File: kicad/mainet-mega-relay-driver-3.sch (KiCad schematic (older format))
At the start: 10 parts, among them J36 Screw_Terminal_01x03, J86 Conn_01x01_Male, J87 Conn_01x01_Male, K3 SANYOU_SRD_Form_C, Q3 2N3904, U4 4N37

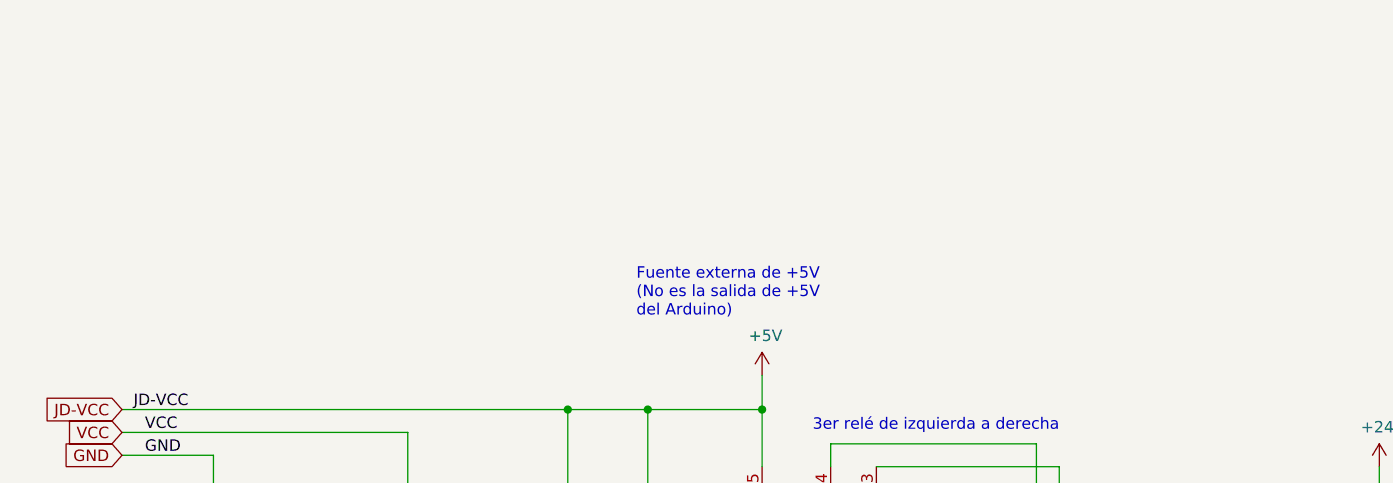
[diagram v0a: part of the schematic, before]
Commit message: KICAD: Actualizar .sch manejadores de relés Agrega alimentación de +5V de dispositivos del lado del Arduino diferente a la salida de +5V del Arduino
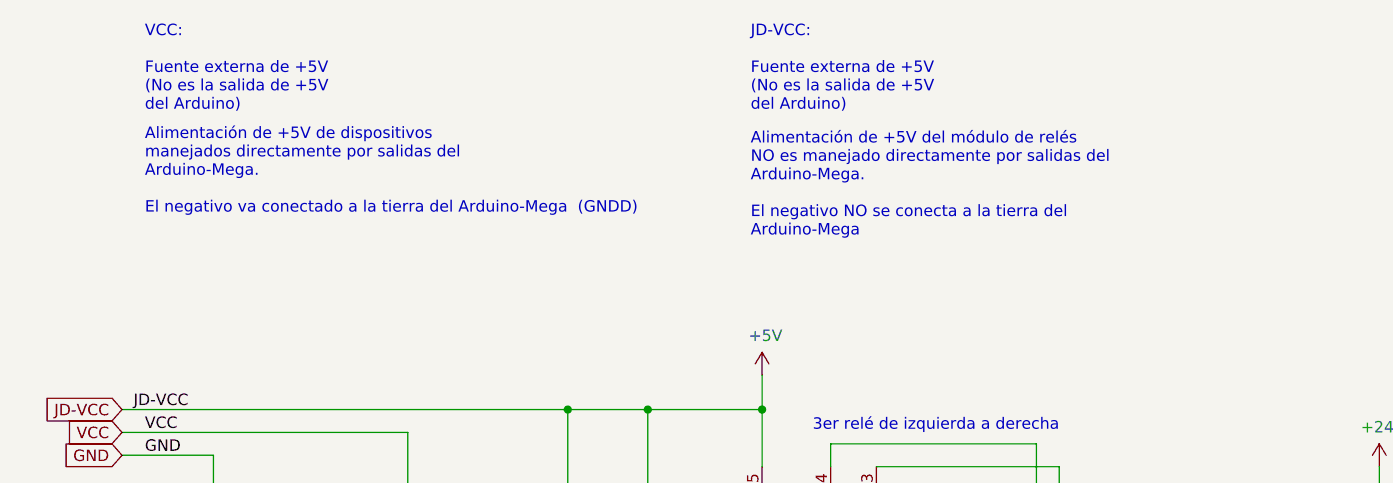
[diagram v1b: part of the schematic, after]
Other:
- note added: "Alimentación de +5V de dispositivos \nmanejados directamente por salidas del \nArduino-Mega.\n\nEl negativo va conectado a la tierra del Arduino-Mega (GNDD)"
- note added: "Alimentación de +5V del módulo de relés \nNO es manejado directamente por salidas del \nArduino-Mega.\n\nEl negativo NO se conecta a la tierra del \nArduino-Mega"
- note added: "JD-VCC:\n\nFuente externa de +5V\n(No es la salida de +5V \ndel Arduino)"
- note added: "VCC:\n\nFuente externa de +5V\n(No es la salida de +5V \ndel Arduino)"
- note removed: "Fuente externa de +5V\n(No es la salida de +5V \ndel Arduino)"
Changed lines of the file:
@@
 	1    0    0    -1
 $EndComp
-Text Notes 5900 2550 0    50   ~ 0
-Fuente externa de +5V\n(No es la salida de +5V \ndel Arduino)
 NoConn ~ 5500 4000
 Wire Wire Line
@@
 Wire Wire Line
 	9150 3300 9150 3700
+Text Notes 6400 1650 0    50   ~ 0
+JD-VCC:\n\nFuente externa de +5V\n(No es la salida de +5V \ndel Arduino)
+Text Notes 3750 1650 0    50   ~ 0
+VCC:\n\nFuente externa de +5V\n(No es la salida de +5V \ndel Arduino)
+Text Notes 3750 2100 0    50   ~ 0
+Alimentación de +5V de dispositivos \nmanejados directamente por salidas del \nArduino-Mega.\n\nEl negativo va conectado a la tierra del Arduino-Mega  (GNDD)
+Text Notes 6400 2200 0    50   ~ 0
+Alimentación de +5V del módulo de relés \nNO es manejado directamente por salidas del \nArduino-Mega.\n\nEl negativo NO se conecta a la tierra del \nArduino-Mega
 $EndSCHEMATC

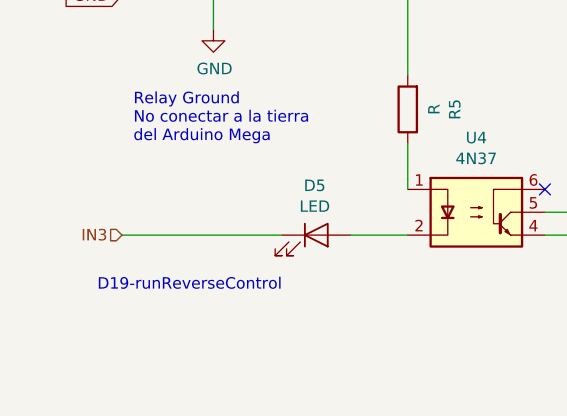
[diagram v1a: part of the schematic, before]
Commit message: KICAD: Corregir numeración pines Arduino de control de relés
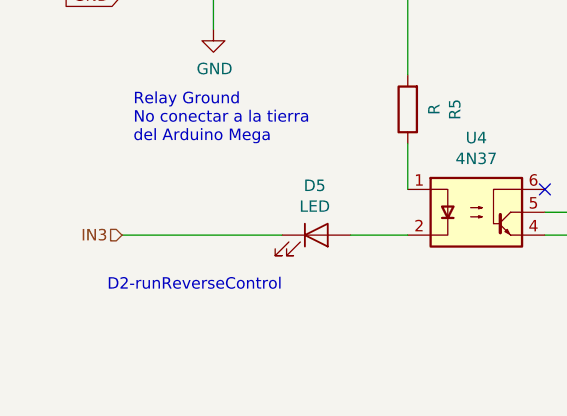
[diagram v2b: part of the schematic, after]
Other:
- note added: "D2-runReverseControl"
- note removed: "D19-runReverseControl"
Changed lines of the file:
@@
 Terminal 13 del M400
 Text Notes 4350 4450 2    50   ~ 0
-D19-runReverseControl
+D2-runReverseControl
 Wire Wire Line
 	3650 3050 4900 3050
